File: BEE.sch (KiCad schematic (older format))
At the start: 40 parts, among them J1 RPI1_header, J10 Conn_01x02, J11 Conn_01x02, J12 Conn_01x02, J13 Conn_01x06, J14 Conn_01x03, J15 Conn_01x03, J16 Conn_01x08, J17 Conn_01x03, J2 Conn_02x05_Odd_Even, J3 Conn_02x03_Odd_Even, J4 Conn_01x06, J5 Conn_02x10_Odd_Even, J6 Conn_02x02_Odd_Even, J7 Conn_02x02_Odd_Even, J8 Conn_01x08, J9 Conn_01x02, SW1 SW_Push, SW2 SW_Push, SW3 SW_Push, U1 MCP3008, U2 MCP4911

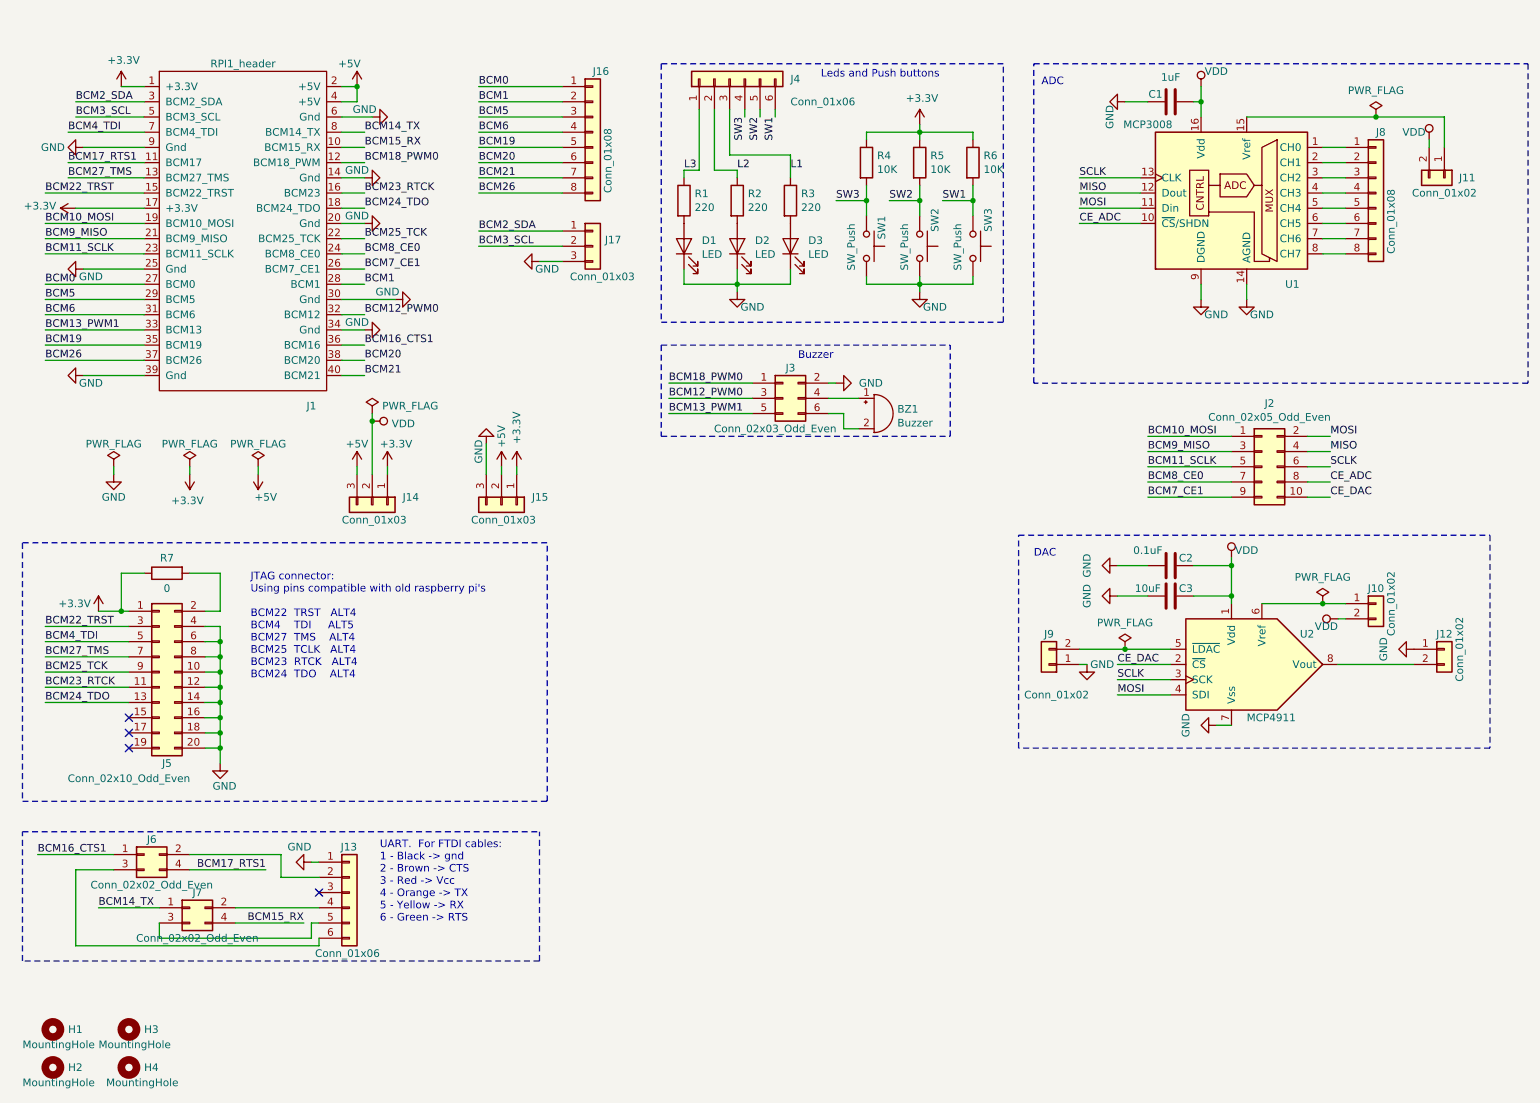
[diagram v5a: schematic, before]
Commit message: reposition, reroute, removed cross connector for UART. Labeled
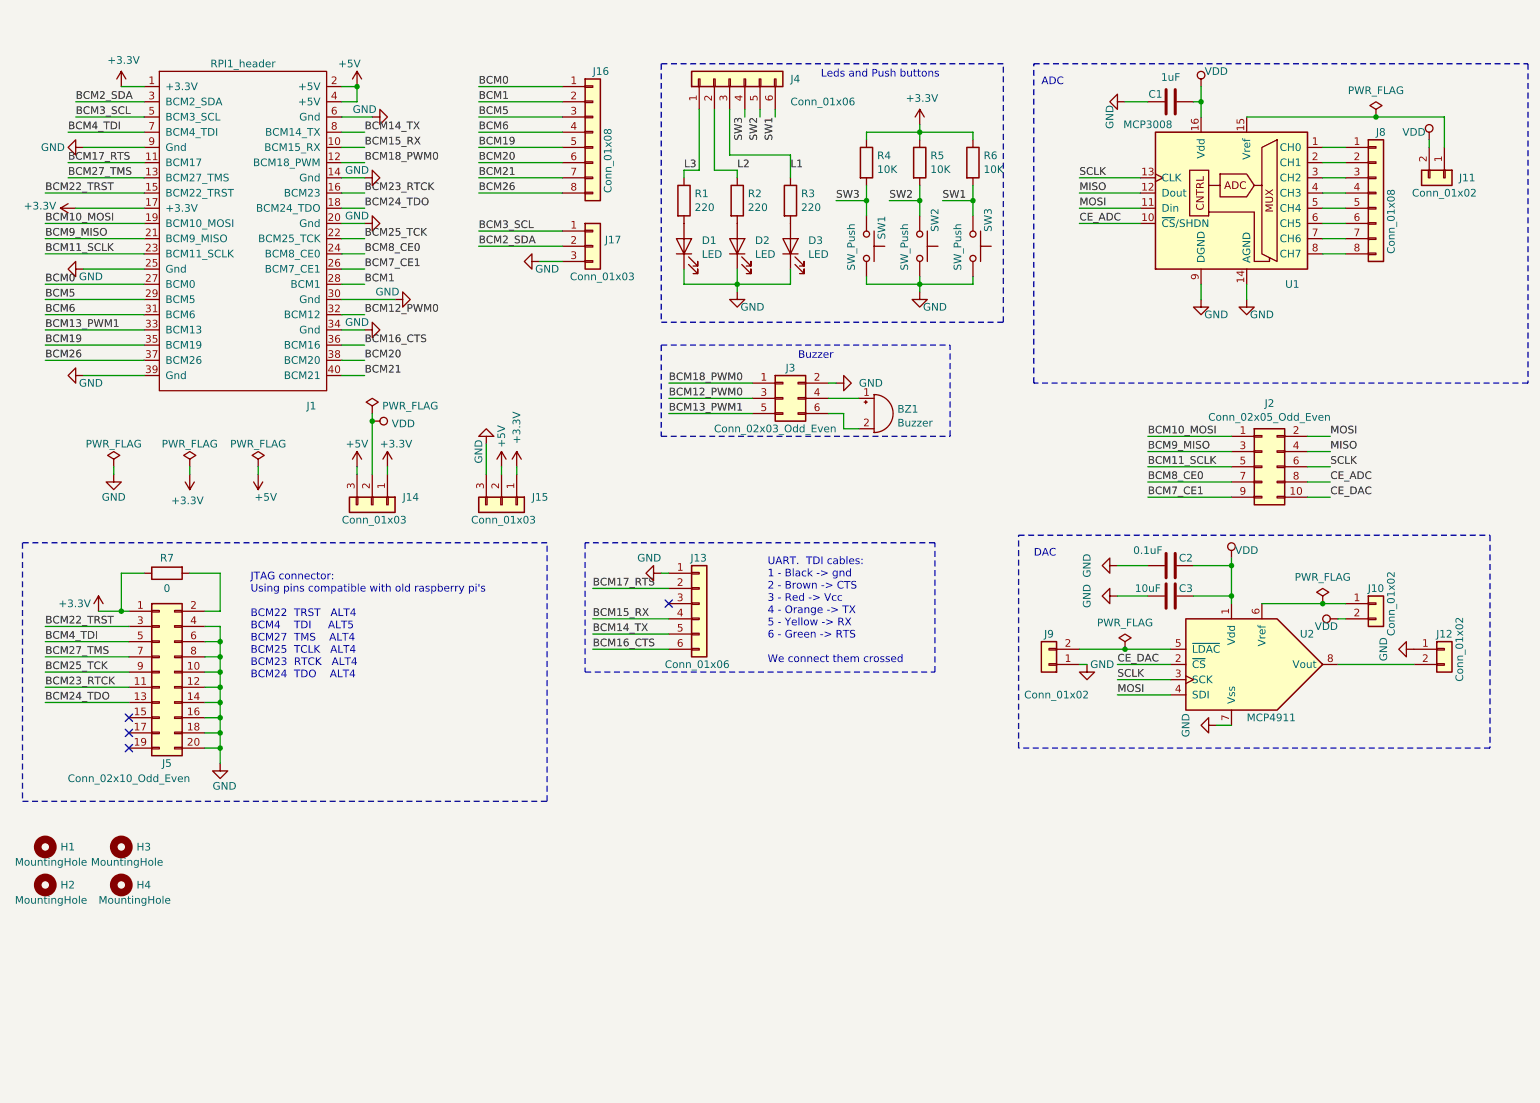
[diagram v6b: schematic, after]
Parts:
- removed J6, J7: Conn_02x02_Odd_Even, Connector_PinHeader_2.54mm:PinHeader_2x02_P2.54mm_Vertical, symbol Connector_Generic:Conn_02x02_Odd_Even
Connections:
- net BCM16_CTS1 is gone; now on net BCM16_CTS: J1.36 (BCM16)
- net BCM17_RTS1 is gone; now on net BCM17_RTS: J1.11 (BCM17)
- net BCM14_TX: now also J13.5 (Pin_5)
- net BCM15_RX: now also J13.4 (Pin_4)
- net BCM2_SDA: now also J17.2 (Pin_2); no longer J17.1 (Pin_1)
- net BCM3_SCL: now also J17.1 (Pin_1); no longer J17.2 (Pin_2)
- net BCM17_RTS: now reaches J13.2 (Pin_2)
- net BCM16_CTS: now reaches J13.6 (Pin_6)
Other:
- note added: "UART. TDI cables:\n1 - Black -> gnd\n2 - Brown -> CTS\n3 - Red -> Vcc\n4 - Orange -> TX\n5 - Yellow -> RX\n6 - Green -> RTS\n\nWe connect them crossed"
- note removed: "UART. For FTDI cables:\n1 - Black -> gnd\n2 - Brown -> CTS\n3 - Red -> Vcc\n4 - Orange -> TX\n5 - Yellow -> RX\n6 - Green -> RTS"
- moved on the sheet: H1, H2, H3, H4, J13
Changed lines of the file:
@@
 	1500 1450 1000 1450
 Text Label 1000 1450 0    50   ~ 0
-BCM17_RTS1
+BCM17_RTS
 Wire Wire Line
 	1000 1550 1500 1550
@@
 Text Label 2950 2150 0    50   ~ 0
 BCM7_CE1
-Text Label 2300 6100 2    50   ~ 0
-BCM17_RTS1
+Text Label 4450 4250 0    50   ~ 0
+BCM17_RTS
+Text Label 3700 2000 0    50   ~ 0
+BCM2_SDA
 Text Label 3700 1900 0    50   ~ 0
-BCM2_SDA
-Text Label 3700 2000 0    50   ~ 0
 BCM3_SCL
 Wire Wire Line
@@
 BCM23_RTCK
 Wire Wire Line
+	3700 1900 4250 1900
+Wire Wire Line
 	3700 2000 4250 2000
-Wire Wire Line
-	2300 6100 1800 6100
-Wire Wire Line
-	3700 1900 4250 1900
-Wire Wire Line
-	1600 6350 1200 6350
-Text Label 1200 6350 0    50   ~ 0
+Text Label 4450 4550 0    50   ~ 0
 BCM14_TX
-Wire Wire Line
-	2100 6450 2550 6450
-Text Label 2550 6450 2    50   ~ 0
+Text Label 4450 4450 0    50   ~ 0
 BCM15_RX
 Text Label 4950 2900 0    50   ~ 0
@@
 	2800 2650 2950 2650
 Text Label 2950 2650 0    50   ~ 0
-BCM16_CTS1
+BCM16_CTS
 Wire Wire Line
 	2800 2750 2950 2750
@@
 BCM19
 Wire Wire Line
-	1300 6000 800  6000
-Text Label 800  6000 0    50   ~ 0
-BCM16_CTS1
+	4950 4650 4450 4650
+Text Label 4450 4650 0    50   ~ 0
+BCM16_CTS
 Text Label 3700 1050 0    50   ~ 0
 BCM1
@@
 Wire Notes Line
 	700  3950 700  5650
-Text Notes 3050 6450 0    50   ~ 0
-UART.  For FTDI cables:\n1 - Black -> gnd\n2 - Brown -> CTS\n3 - Red -> Vcc\n4 - Orange -> TX\n5 - Yellow -> RX\n6 - Green -> RTS
+Text Notes 5600 4750 0    50   ~ 0
+UART.  TDI cables:\n1 - Black -> gnd\n2 - Brown -> CTS\n3 - Red -> Vcc\n4 - Orange -> TX\n5 - Yellow -> RX\n6 - Green -> RTS\n\nWe connect them crossed
 $Comp
 L Connector_Generic:Conn_01x06 J13
 U 1 1 5D9CD8D7
-P 2850 6250
-F 0 "J13" H 2900 6550 50  0000 R CNN
-F 1 "Conn_01x06" H 3050 5850 50  0000 R CNN
-F 2 "Connector_PinHeader_2.54mm:PinHeader_1x06_P2.54mm_Vertical" H 2850 6250 50  0001 C CNN
-F 3 "https://www.mouser.es/datasheet/2/276/0022284060_PCB_HEADERS-228129.pdf" H 2850 6250 50  0001 C CNN
-F 4 "Mouser" H -2500 5350 50  0001 C CNN "Distributor"
-F 5 " 538-22-28-4060 " H -2500 5350 50  0001 C CNN "Distributor PN"
-F 6 "https://www.mouser.es/ProductDetail/Molex/22-28-4060?qs=sGAEpiMZZMs%252BGHln7q6pm%252BS0pk2Wo0XxC4Xq7BDQXEY%3D" H -2500 5350 50  0001 C CNN "Distributor link"
-F 7 "Molex" H -2500 5350 50  0001 C CNN "Manufacturer"
-F 8 "22-28-4060" H -2500 5350 50  0001 C CNN "Manufacturer PN"
-	1    2850 6250
+P 5150 4350
+F 0 "J13" H 5200 4650 50  0000 R CNN
+F 1 "Conn_01x06" H 5350 3950 50  0000 R CNN
+F 2 "Connector_PinHeader_2.54mm:PinHeader_1x06_P2.54mm_Vertical" H 5150 4350 50  0001 C CNN
+F 3 "https://www.mouser.es/datasheet/2/276/0022284060_PCB_HEADERS-228129.pdf" H 5150 4350 50  0001 C CNN
+F 4 "Mouser" H -200 3450 50  0001 C CNN "Distributor"
+F 5 " 538-22-28-4060 " H -200 3450 50  0001 C CNN "Distributor PN"
+F 6 "https://www.mouser.es/ProductDetail/Molex/22-28-4060?qs=sGAEpiMZZMs%252BGHln7q6pm%252BS0pk2Wo0XxC4Xq7BDQXEY%3D" H -200 3450 50  0001 C CNN "Distributor link"
+F 7 "Molex" H -200 3450 50  0001 C CNN "Manufacturer"
+F 8 "22-28-4060" H -200 3450 50  0001 C CNN "Manufacturer PN"
+	1    5150 4350
 	1    0    0    -1
 $EndComp
@@
 L power:GND #PWR0108
 U 1 1 5DA0B7FD
-P 2600 6050
-F 0 "#PWR0108" H 2600 5800 50  0001 C CNN
-F 1 "GND" V 2500 6050 50  0000 R CNN
-F 2 "" H 2600 6050 50  0001 C CNN
-F 3 "" H 2600 6050 50  0001 C CNN
-	1    2600 6050
+P 4900 4150
+F 0 "#PWR0108" H 4900 3900 50  0001 C CNN
+F 1 "GND" V 4800 4150 50  0000 R CNN
+F 2 "" H 4900 4150 50  0001 C CNN
+F 3 "" H 4900 4150 50  0001 C CNN
+	1    4900 4150
 	0    1    1    0
 $EndComp
 Wire Wire Line
-	2600 6050 2650 6050
-NoConn ~ 2650 6250
-Wire Notes Line
-	4100 6700 4100 5850
+	4900 4150 4950 4150
+NoConn ~ 4950 4350
 $Comp
 L Mechanical:MountingHole H1
 U 1 1 5DACDC65
-P 900 7150
-F 0 "H1" H 1000 7150 50  0000 L CNN
-F 1 "MountingHole" H 700 7050 50  0000 L CNN
-F 2 "MountingHole:MountingHole_2.5mm" H 900 7150 50  0001 C CNN
-F 3 "~" H 900 7150 50  0001 C CNN
-	1    900  7150
+P 850 5950
+F 0 "H1" H 950 5950 50  0000 L CNN
+F 1 "MountingHole" H 650 5850 50  0000 L CNN
+F 2 "MountingHole:MountingHole_2.5mm" H 850 5950 50  0001 C CNN
+F 3 "~" H 850 5950 50  0001 C CNN
+	1    850  5950
 	1    0    0    -1
 $EndComp
@@
 L Mechanical:MountingHole H2
 U 1 1 5DACDD9A
-P 900 7400
-F 0 "H2" H 1000 7400 50  0000 L CNN
-F 1 "MountingHole" H 700 7300 50  0000 L CNN
-F 2 "MountingHole:MountingHole_2.5mm" H 900 7400 50  0001 C CNN
-F 3 "~" H 900 7400 50  0001 C CNN
-	1    900  7400
+P 850 6200
+F 0 "H2" H 950 6200 50  0000 L CNN
+F 1 "MountingHole" H 650 6100 50  0000 L CNN
+F 2 "MountingHole:MountingHole_2.5mm" H 850 6200 50  0001 C CNN
+F 3 "~" H 850 6200 50  0001 C CNN
+	1    850  6200
 	1    0    0    -1
 $EndComp
@@
 L Mechanical:MountingHole H4
 U 1 1 5DACDDF8
-P 1400 7400
-F 0 "H4" H 1500 7400 50  0000 L CNN
-F 1 "MountingHole" H 1250 7300 50  0000 L CNN
-F 2 "MountingHole:MountingHole_2.5mm" H 1400 7400 50  0001 C CNN
-F 3 "~" H 1400 7400 50  0001 C CNN
-	1    1400 7400
+P 1350 6200
+F 0 "H4" H 1450 6200 50  0000 L CNN
+F 1 "MountingHole" H 1200 6100 50  0000 L CNN
+F 2 "MountingHole:MountingHole_2.5mm" H 1350 6200 50  0001 C CNN
+F 3 "~" H 1350 6200 50  0001 C CNN
+	1    1350 6200
 	1    0    0    -1
 $EndComp
@@
 L Mechanical:MountingHole H3
 U 1 1 5DACDE80
-P 1400 7150
-F 0 "H3" H 1500 7150 50  0000 L CNN
-F 1 "MountingHole" H 1200 7050 50  0000 L CNN
-F 2 "MountingHole:MountingHole_2.5mm" H 1400 7150 50  0001 C CNN
-F 3 "~" H 1400 7150 50  0001 C CNN
-	1    1400 7150
+P 1350 5950
+F 0 "H3" H 1450 5950 50  0000 L CNN
+F 1 "MountingHole" H 1150 5850 50  0000 L CNN
+F 2 "MountingHole:MountingHole_2.5mm" H 1350 5950 50  0001 C CNN
+F 3 "~" H 1350 5950 50  0001 C CNN
+	1    1350 5950
 	1    0    0    -1
 $EndComp
@@
 	4100 2100 4250 2100
 $Comp
-L Connector_Generic:Conn_02x02_Odd_Even J7
-U 1 1 5DCD26D5
-P 1800 6350
-F 0 "J7" H 1850 6450 50  0000 C CNN
-F 1 "Conn_02x02_Odd_Even" H 1850 6150 50  0000 C CNN
-F 2 "Connector_PinHeader_2.54mm:PinHeader_2x02_P2.54mm_Vertical" H 1800 6350 50  0001 C CNN
-F 3 "https://www.mouser.es/datasheet/2/18/67996-1142923.pdf" H 1800 6350 50  0001 C CNN
-F 4 "Mouser" H 0   0   50  0001 C CNN "Distributor"
-F 5 "649-67997-404HLF " H 0   0   50  0001 C CNN "Distributor PN"
-F 6 "https://www.mouser.es/ProductDetail/Amphenol-FCI/67997-404HLF?qs=sGAEpiMZZMs%252BGHln7q6pm2nKUjHUi6l6x1G9%252BQjC1vk%3D" H 0   0   50  0001 C CNN "Distributor link"
-F 7 "Amphenol FCI" H 0   0   50  0001 C CNN "Manufacturer"
-F 8 "67997-404HLF" H 0   0   50  0001 C CNN "Manufacturer PN"
-	1    1800 6350
-	1    0    0    -1
-$EndComp
-Wire Wire Line
-	2100 6350 2650 6350
-Wire Wire Line
-	1600 6450 1600 6550
-Wire Wire Line
-	1600 6550 2600 6550
-Wire Wire Line
-	2600 6550 2600 6450
-Wire Wire Line
-	2600 6450 2650 6450
-$Comp
-L Connector_Generic:Conn_02x02_Odd_Even J6
-U 1 1 5DDCFADD
-P 1500 6000
-F 0 "J6" H 1550 6100 50  0000 C CNN
-F 1 "Conn_02x02_Odd_Even" H 1550 5800 50  0000 C CNN
-F 2 "Connector_PinHeader_2.54mm:PinHeader_2x02_P2.54mm_Vertical" H 1500 6000 50  0001 C CNN
-F 3 "https://www.mouser.es/datasheet/2/18/67996-1142923.pdf" H 1500 6000 50  0001 C CNN
-F 4 "Mouser" H 0   0   50  0001 C CNN "Distributor"
-F 5 "649-67997-404HLF " H 0   0   50  0001 C CNN "Distributor PN"
-F 6 "https://www.mouser.es/ProductDetail/Amphenol-FCI/67997-404HLF?qs=sGAEpiMZZMs%252BGHln7q6pm2nKUjHUi6l6x1G9%252BQjC1vk%3D" H 0   0   50  0001 C CNN "Distributor link"
-F 7 "Amphenol FCI" H 0   0   50  0001 C CNN "Manufacturer"
-F 8 "67997-404HLF" H 0   0   50  0001 C CNN "Manufacturer PN"
-	1    1500 6000
-	1    0    0    -1
-$EndComp
-Wire Wire Line
-	2650 6150 2400 6150
-Wire Wire Line
-	2400 6150 2400 6000
-Wire Wire Line
-	2400 6000 1800 6000
-Wire Wire Line
-	1300 6100 1050 6100
-Wire Wire Line
-	1050 6100 1050 6600
-Wire Wire Line
-	1050 6600 2650 6600
-Wire Wire Line
-	2650 6600 2650 6550
-Wire Notes Line
-	4100 6700 700  6700
-Wire Notes Line
-	700  6700 700  5850
-Wire Notes Line
-	700  5850 4100 5850
-$Comp
 L Connector_Generic:Conn_01x08 J16
 U 1 1 5DED01C3
@@
 	1    0    0    -1
 $EndComp
+Wire Wire Line
+	4450 4450 4950 4450
+Wire Wire Line
+	4450 4550 4950 4550
+Wire Wire Line
+	4450 4250 4950 4250
+Wire Notes Line
+	4400 3950 4400 4800
+Wire Notes Line
+	4400 4800 6700 4800
+Wire Notes Line
+	6700 4800 6700 3950
+Wire Notes Line
+	6700 3950 4400 3950
 $EndSCHEMATC

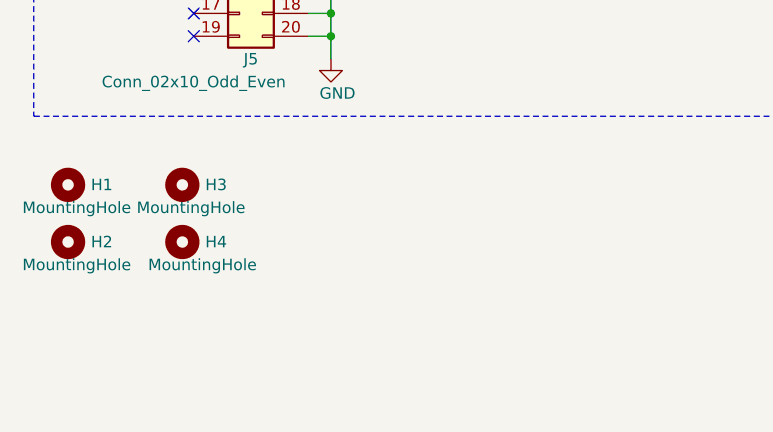
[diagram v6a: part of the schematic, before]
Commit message: Fiducials and Logos
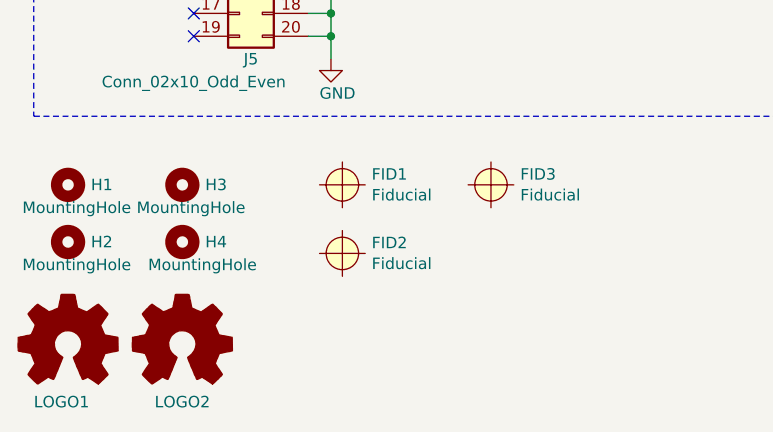
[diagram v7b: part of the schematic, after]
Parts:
- added FID1, FID2, FID3: Fiducial, Fiducial:Fiducial_0.5mm_Dia_1mm_Outer, symbol BEE:Fiducial
- added LOGO1: Logo_Open_Hardware_Small, Symbol:OSHW-Logo2_7.3x6mm_SilkScreen, symbol Graphic:Logo_Open_Hardware_Small
- added LOGO2: Logo_Open_Hardware_Small, BEElib:bee_logo, symbol Graphic:Logo_Open_Hardware_Small
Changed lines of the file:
@@
 Wire Notes Line
 	6700 3950 4400 3950
+$Comp
+L BEE:Fiducial FID1
+U 1 1 5E028B4F
+P 2050 5950
+F 0 "FID1" H 2178 5996 50  0000 L CNN
+F 1 "Fiducial" H 2178 5905 50  0000 L CNN
+F 2 "Fiducial:Fiducial_0.5mm_Dia_1mm_Outer" H 2050 5950 50  0001 C CNN
+F 3 "" H 2050 5950 50  0001 C CNN
+	1    2050 5950
+	1    0    0    -1
+$EndComp
+$Comp
+L BEE:Fiducial FID2
+U 1 1 5E028C55
+P 2050 6250
+F 0 "FID2" H 2178 6296 50  0000 L CNN
+F 1 "Fiducial" H 2178 6205 50  0000 L CNN
+F 2 "Fiducial:Fiducial_0.5mm_Dia_1mm_Outer" H 2050 6250 50  0001 C CNN
+F 3 "" H 2050 6250 50  0001 C CNN
+	1    2050 6250
+	1    0    0    -1
+$EndComp
+$Comp
+L BEE:Fiducial FID3
+U 1 1 5E028CC1
+P 2700 5950
+F 0 "FID3" H 2828 5996 50  0000 L CNN
+F 1 "Fiducial" H 2828 5905 50  0000 L CNN
+F 2 "Fiducial:Fiducial_0.5mm_Dia_1mm_Outer" H 2700 5950 50  0001 C CNN
+F 3 "" H 2700 5950 50  0001 C CNN
+	1    2700 5950
+	1    0    0    -1
+$EndComp
+$Comp
+L Graphic:Logo_Open_Hardware_Small LOGO1
+U 1 1 5E029178
+P 850 6650
+F 0 "LOGO1" H 700 6400 50  0000 L CNN
+F 1 "Logo_Open_Hardware_Small" H 850 6425 50  0001 C CNN
+F 2 "Symbol:OSHW-Logo2_7.3x6mm_SilkScreen" H 850 6650 50  0001 C CNN
+F 3 "~" H 850 6650 50  0001 C CNN
+	1    850  6650
+	1    0    0    -1
+$EndComp
+$Comp
+L Graphic:Logo_Open_Hardware_Small LOGO2
+U 1 1 5E0293AA
+P 1350 6650
+F 0 "LOGO2" H 1350 6400 50  0000 C CNN
+F 1 "Logo_Open_Hardware_Small" H 1350 6425 50  0001 C CNN
+F 2 "BEElib:bee_logo" H 1350 6650 50  0001 C CNN
+F 3 "~" H 1350 6650 50  0001 C CNN
+	1    1350 6650
+	1    0    0    -1
+$EndComp
 $EndSCHEMATC

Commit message: UCM logo and github repo url
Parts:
- added LOGO3: Logo_Open_Hardware_Small, BEElib:UCMLogo_169_169, symbol Graphic:Logo_Open_Hardware_Small
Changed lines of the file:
@@
+	1    0    0    -1
+$EndComp
+$Comp
+L Graphic:Logo_Open_Hardware_Small LOGO3
+U 1 1 5E02C6EE
+P 1900 6650
+F 0 "LOGO3" H 1900 6400 50  0000 C CNN
+F 1 "Logo_Open_Hardware_Small" H 1900 6425 50  0001 C CNN
+F 2 "BEElib:UCMLogo_169_169" H 1900 6650 50  0001 C CNN
+F 3 "~" H 1900 6650 50  0001 C CNN
+	1    1900 6650
 	1    0    0    -1
 $EndComp
